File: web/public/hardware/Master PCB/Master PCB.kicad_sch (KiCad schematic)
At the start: 28 parts, among them J1 Rows 0-15, J10 LDR2, J11 LDR3, J12 LDR4, J13 SWD Conn, J14 LED Conn, J15 OLED1, J16 OLED2, J17 Relay Conn, J2 Cols 0-21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

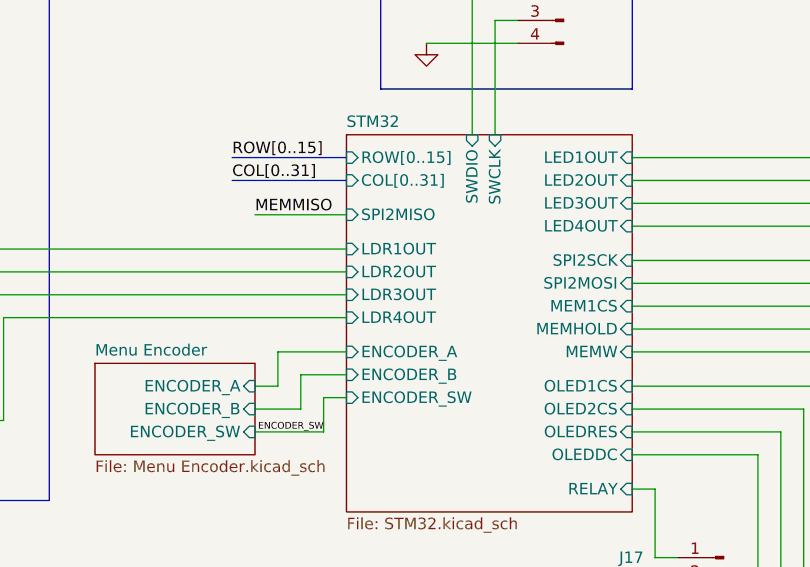
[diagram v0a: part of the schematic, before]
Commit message: Rename nets for clarity
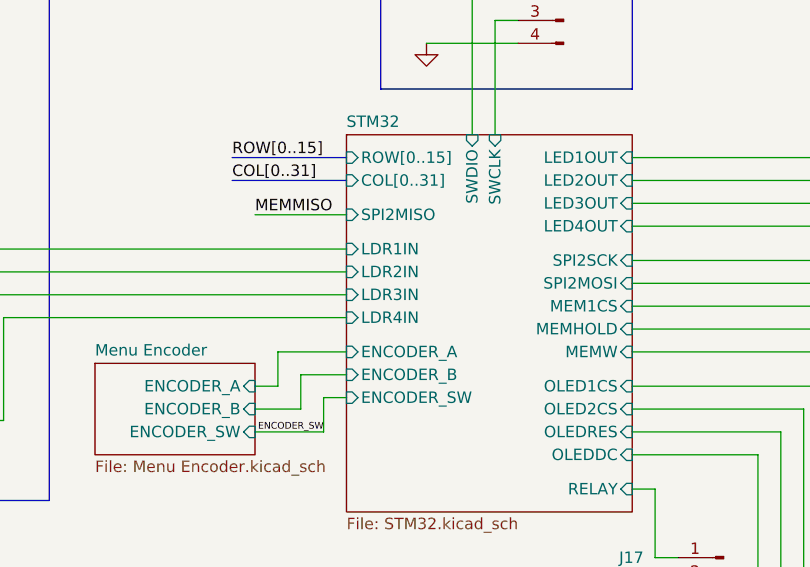
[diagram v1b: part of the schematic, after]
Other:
- sheet STM32 ports: added LDR1IN, LDR2IN, LDR3IN, LDR4IN; removed LDR1OUT, LDR2OUT, LDR3OUT, LDR4OUT
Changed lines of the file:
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@@
-      (effects (font (size 1.27 1.27)) (justify left))
-    )
-    (pin "LDR1OUT" input (at 160.02 67.31 180)
-      (effects (font (size 1.27 1.27)) (justify left))
-    )
-    (pin "LDR2OUT" input (at 160.02 69.85 180)
-      (effects (font (size 1.27 1.27)) (justify left))
-    )
-    (pin "LDR3OUT" input (at 160.02 72.39 180)
-      (effects (font (size 1.27 1.27)) (justify left))
-    )
-    (pin "LDR4OUT" input (at 160.02 74.93 180)
       (effects (font (size 1.27 1.27)) (justify left))
     )
@@
       (effects (font (size 1.27 1.27)) (justify right))
     )
+    (pin "LDR1IN" input (at 160.02 67.31 180)
+      (effects (font (size 1.27 1.27)) (justify left))
+    )
+    (pin "LDR4IN" input (at 160.02 74.93 180)
+      (effects (font (size 1.27 1.27)) (justify left))
+    )
+    (pin "LDR2IN" input (at 160.02 69.85 180)
+      (effects (font (size 1.27 1.27)) (justify left))
+    )
+    (pin "LDR3IN" input (at 160.02 72.39 180)
+      (effects (font (size 1.27 1.27)) (justify left))
+    )
     (instances

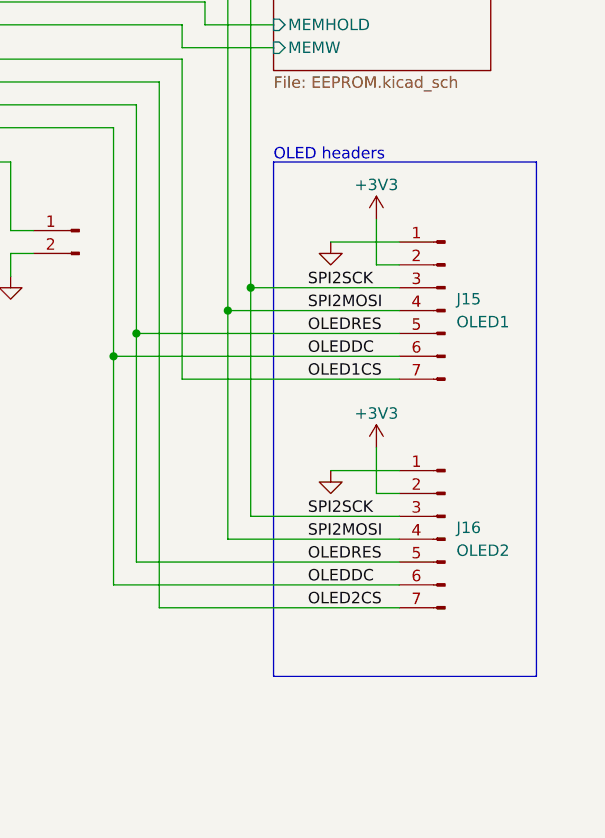
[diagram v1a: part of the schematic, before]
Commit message: Fix encoder schematic and miscellaneous cleanup (new date, etc.)
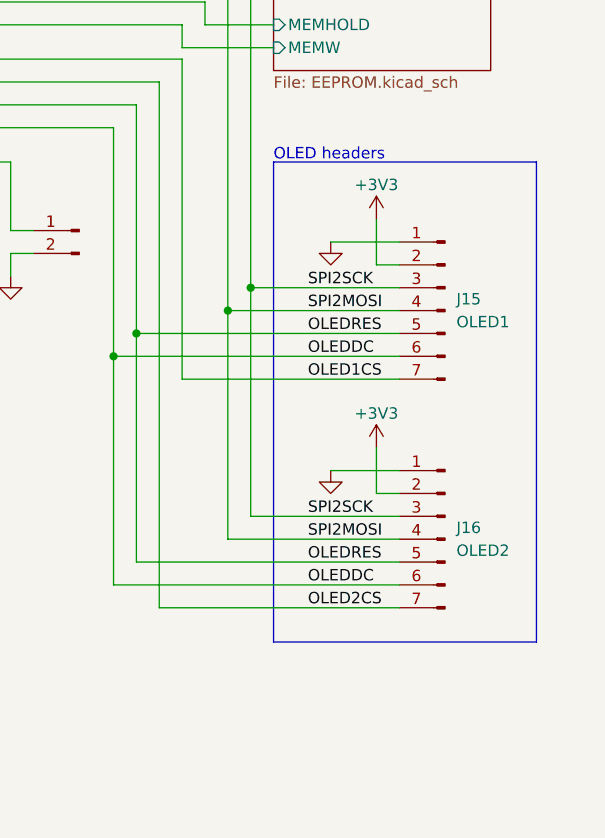
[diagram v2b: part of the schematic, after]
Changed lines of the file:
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@@
   (title_block
     (title "Smart Air Hockey Table Master PCB")
-    (date "2023-09-16")
-    (rev "A")
+    (date "2023-10-08")
+    (rev "B")
     (company "ECE 477")
   )
@@
     (fill (type none))
   )
-  (rectangle (start 223.52 93.98) (end 252.73 151.13)
+  (rectangle (start 223.52 93.98) (end 252.73 147.32)
     (stroke (width 0) (type default))
     (fill (type none))
